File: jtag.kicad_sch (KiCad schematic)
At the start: 0 parts

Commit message: jtag.kicad_sch: add Conn_JTAG_20
Signed-off-by: Huang Rui <vowstar@gmail.com>
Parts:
- added C1 (x2): 100n, Capacitor_SMD:C_0402_1005Metric, symbol Device:C
- added J5: Conn_JTAG_20, Connector_IDC:IDC-Header_2x10_P2.54mm_Vertical, symbol CHIPSAlliance_Connector:Conn_JTAG_20
- added U4: SN74LVC1T45DBV, Package_TO_SOT_SMD:SOT-23-6, symbol CHIPSAlliance_Logic:SN74LVC1T45DBV
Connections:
- new net GND: C1.2, C1.2, J5.10 (GND), J5.12 (GND), J5.14 (GND), J5.16 (GND), J5.18 (GND), J5.20 (GND), J5.4 (GND), J5.6 (GND), J5.8 (GND), U4.2 (GND), U4.5 (DIR)
- new net JTAG.TDO: U4.4 (B)
- new net VDD: C1.1, C1.1, U4.1 (VCCA), U4.6 (VCCB)

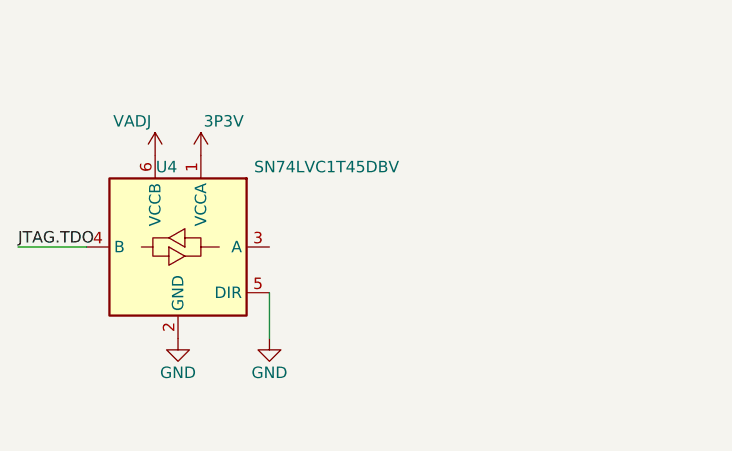
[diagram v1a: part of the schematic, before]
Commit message: *.kicad_sch: changed SN74LVC1T45DBV to symbol AIP74LVC1T45GB236TR
Signed-off-by: Huang Rui <vowstar@gmail.com>
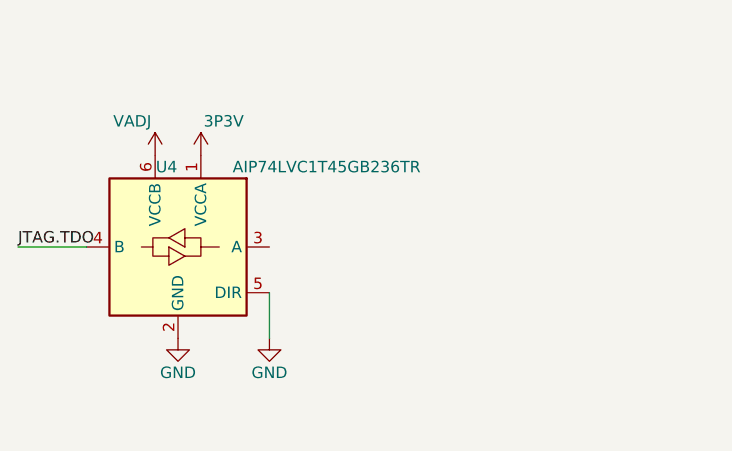
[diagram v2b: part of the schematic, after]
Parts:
- U4: value SN74LVC1T45DBV -> AIP74LVC1T45GB236TR; symbol CHIPSAlliance_Logic:SN74LVC1T45DBV -> CHIPSAlliance_Logic:AIP74LVC1T45GB236TR
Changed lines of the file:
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@@
     )
   )
-  (symbol (lib_id "CHIPSAlliance_Logic:SN74LVC1T45DBV") (at 60.96 82.55 0) (mirror y) (unit 1)
+  (symbol (lib_id "CHIPSAlliance_Logic:AIP74LVC1T45GB236TR") (at 60.96 82.55 0) (mirror y) (unit 1)
     (in_bom yes) (on_board yes) (dnp no)
     (property "Reference" "U4" (at 52.07 81.28 0)
       (effects (font (size 1.27 1.27)))
     )
-    (property "Value" "SN74LVC1T45DBV" (at 69.85 81.28 0)
+    (property "Value" "AIP74LVC1T45GB236TR" (at 69.85 81.28 0)
       (effects (font (size 1.27 1.27)))
     )
     (property "Footprint" "Package_TO_SOT_SMD:SOT-23-6" (at 60.96 93.98 0)
-      (effects (font (size 1.27 1.27)) hide)
+      (effects (font (size 1.27 1.27)) (justify left) hide)
     )
-    (property "Datasheet" "http://www.ti.com/lit/ds/symlink/sn74lvc1t45.pdf" (at 83.82 99.06 0)
-      (effects (font (size 1.27 1.27)) hide)
+    (property "Datasheet" "https://atta.szlcsc.com/upload/public/pdf/source/20220915/C3F384B245F14B1C45E49B7D1719C9B2.pdf" (at 83.82 99.06 0)
+      (effects (font (size 1.27 1.27)) (justify left) hide)
     )
     (property "JLCPCB Rotation Offset" "-180" (at 60.96 106.68 0)

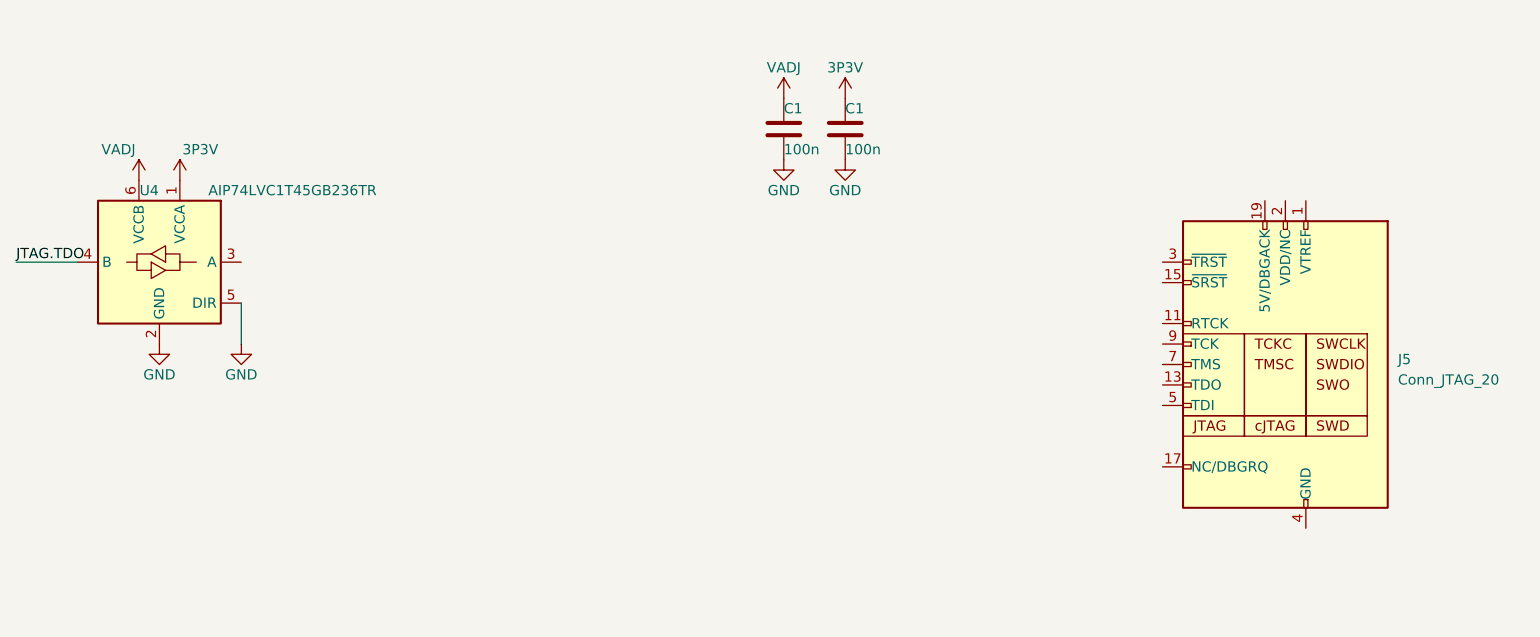
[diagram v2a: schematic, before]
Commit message: jtag.kicad_sch: use TXS02612RTWR as level shifter
Signed-off-by: Huang Rui <vowstar@gmail.com>
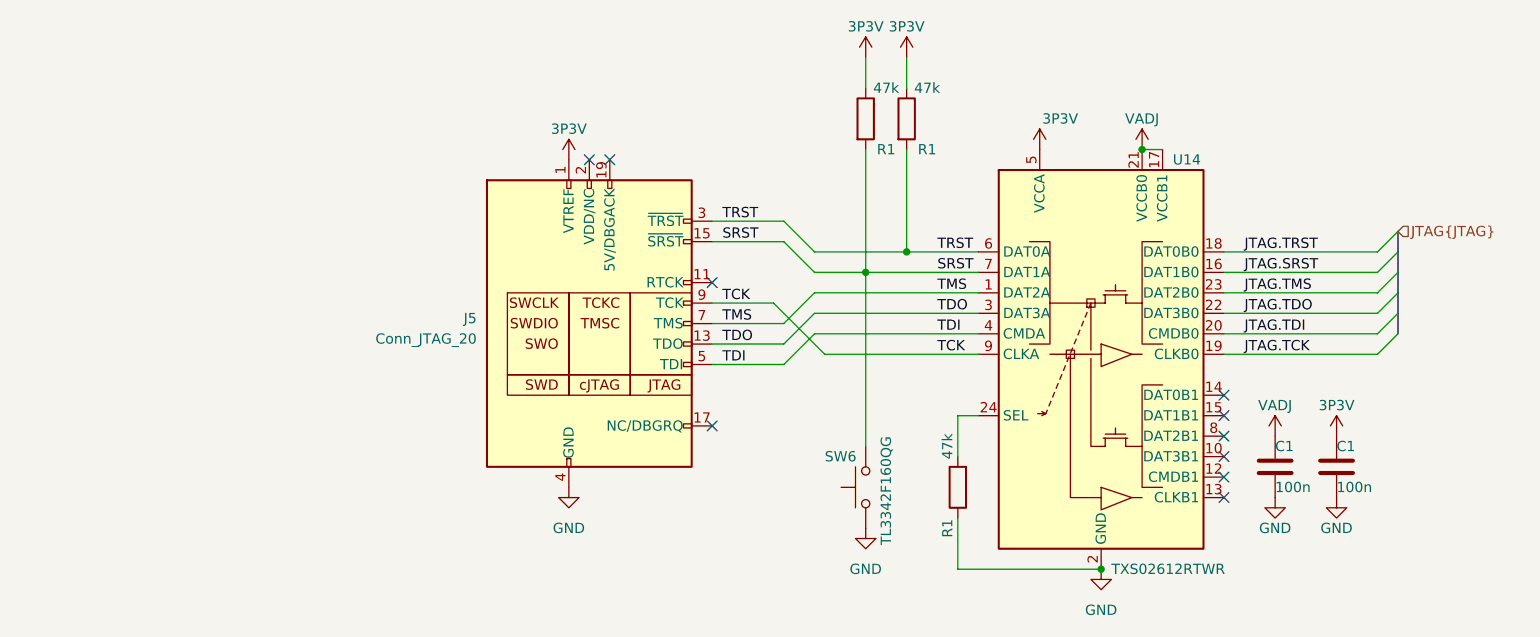
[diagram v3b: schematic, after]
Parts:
- removed U4: AIP74LVC1T45GB236TR, Package_TO_SOT_SMD:SOT-23-6, symbol CHIPSAlliance_Logic:AIP74LVC1T45GB236TR
- added R1 (x3): 47k, Resistor_SMD:R_0402_1005Metric, symbol Device:R
- added SW6: TL3342F160QG, Button_Switch_SMD:SW_SPST_TL3342, symbol Switch:SW_Push
- added U14: TXS02612RTWR, Package_DFN_QFN:WQFN-24-1EP_4x4mm_P0.5mm_EP2.45x2.45mm, symbol CHIPSAlliance_Logic:TXS02612RTWR
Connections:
- net GND: now also R1.1, SW6.1, U14.11 (GND), U14.2 (GND)
- net JTAG.TDO: now also U14.22 (DAT3B0)
- net VDD: now also J5.1 (VTREF), R1.1, R1.1, U14.17 (VCCB1), U14.21 (VCCB0), U14.5 (VCCA)
- net TDO: now reaches J5.13 (TDO)
- net TDO: now also U14.3 (DAT3A)
- net SRST: now reaches J5.15 (~{SRST})
- net SRST: now also R1.2, SW6.2, U14.7 (DAT1A)
- net TRST: now reaches J5.3 (~{TRST})
- net TRST: now also R1.2, U14.6 (DAT0A)
- net TDI: now reaches J5.5 (TDI)
- net TDI: now also U14.4 (CMDA)
- net TMS: now reaches J5.7 (TMS)
- net TMS: now also U14.1 (DAT2A)
- net TCK: now reaches J5.9 (TCK)
- net TCK: now also U14.9 (CLKA)
- new net: R1.2, U14.24 (SEL)
- new net JTAG.SRST: U14.16 (DAT1B0)
- new net JTAG.TCK: U14.19 (CLKB0)
- new net JTAG.TDI: U14.20 (CMDB0)
- new net JTAG.TMS: U14.23 (DAT2B0)
- new net JTAG.TRST: U14.18 (DAT0B0)
- no-connect marks 0 -> 10
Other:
- moved on the sheet: C1, J5

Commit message: *.kicad_sch: fix TXS02612RTWR symbols
Signed-off-by: Huang Rui <vowstar@gmail.com>
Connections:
- net GND: now also U14.25 (GND)
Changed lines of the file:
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@@
     (pin "9")
     (pin "1")
+    (pin "25")
     (pin "3")
     (pin "4")

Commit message: jtag.kicad_sch: fix TRST and SRST polarity
Signed-off-by: Huang Rui <vowstar@gmail.com>
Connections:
- net JTAG.SRST renamed JTAG.~{SRST}
- net JTAG.TRST renamed JTAG.~{TRST}
- net SRST renamed ~{SRST}
- net TRST renamed ~{TRST}
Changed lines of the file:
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@@
 (kicad_sch (version 20230121) (generator eeschema)
   (paper "A4")
-  (bus_alias "JTAG" (members "TRST" "SRST" "TMS" "TDO" "TDI" "TCK"))
+  (bus_alias "JTAG" (members "~{TRST}" "~{SRST}" "TMS" "TDO" "TDI" "TCK"))
   (junction (at 140.97 91.44) (diameter 0) (color 0 0 0 0)
   )
@@
     (effects (font (size 1.27 1.27)) (justify left bottom))
   )
-  (label "SRST" (at 123.19 87.63 0) (fields_autoplaced)
-    (effects (font (size 1.27 1.27)) (justify left bottom))
-  )
-  (label "TRST" (at 149.86 88.9 0) (fields_autoplaced)
+  (label "~{SRST}" (at 123.19 87.63 0) (fields_autoplaced)
+    (effects (font (size 1.27 1.27)) (justify left bottom))
+  )
+  (label "~{TRST}" (at 149.86 88.9 0) (fields_autoplaced)
     (effects (font (size 1.27 1.27)) (justify left bottom))
   )
@@
     (effects (font (size 1.27 1.27)) (justify left bottom))
   )
-  (label "JTAG.SRST" (at 187.96 91.44 0) (fields_autoplaced)
-    (effects (font (size 1.27 1.27)) (justify left bottom))
-  )
-  (label "SRST" (at 149.86 91.44 0) (fields_autoplaced)
+  (label "JTAG.~{SRST}" (at 187.96 91.44 0) (fields_autoplaced)
+    (effects (font (size 1.27 1.27)) (justify left bottom))
+  )
+  (label "~{SRST}" (at 149.86 91.44 0) (fields_autoplaced)
     (effects (font (size 1.27 1.27)) (justify left bottom))
   )
@@
     (effects (font (size 1.27 1.27)) (justify left bottom))
   )
-  (label "TRST" (at 123.19 85.09 0) (fields_autoplaced)
+  (label "~{TRST}" (at 123.19 85.09 0) (fields_autoplaced)
     (effects (font (size 1.27 1.27)) (justify left bottom))
   )
@@
     (effects (font (size 1.27 1.27)) (justify left bottom))
   )
-  (label "JTAG.TRST" (at 187.96 88.9 0) (fields_autoplaced)
-    (effects (font (size 1.27 1.27)) (justify left bottom))
-  )
+  (label "JTAG.~{TRST}" (at 187.96 88.9 0) (fields_autoplaced)
+    (effects (font (size 1.27 1.27)) (justify left bottom))
+  )

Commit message: *.kicad_sch: fix sheet pin type
Signed-off-by: Huang Rui <vowstar@gmail.com>
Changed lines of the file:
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@@
     (effects (font (size 1.27 1.27)) (justify left bottom))
   )
-  (hierarchical_label "JTAG{JTAG}" (shape input) (at 207.01 86.36 0) (fields_autoplaced)
+  (hierarchical_label "JTAG{JTAG}" (shape bidirectional) (at 207.01 86.36 0) (fields_autoplaced)
     (effects (font (size 1.27 1.27)) (justify left))
   )
